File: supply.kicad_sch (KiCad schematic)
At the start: 64 parts, among them J3 Molex_Nano-Fit_1x2_SMD_105430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, Q2 SSM3J332R, Q3 SSM3J332R, Q4 BCM857BS-7-F, Q5 BCM857BS-7-F, Q6 SSM3J332R, Q8 PJE138K, Q9 SSM3J332R, U1 TPS56C230

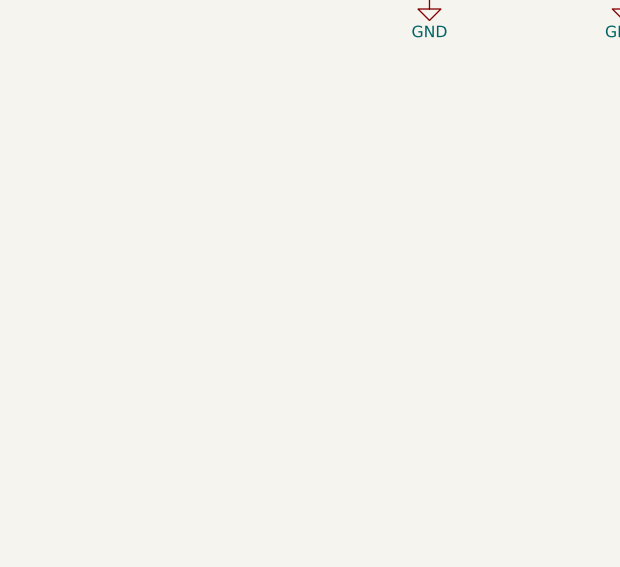
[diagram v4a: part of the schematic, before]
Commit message: [#54474] Change sheet placement in top sheet
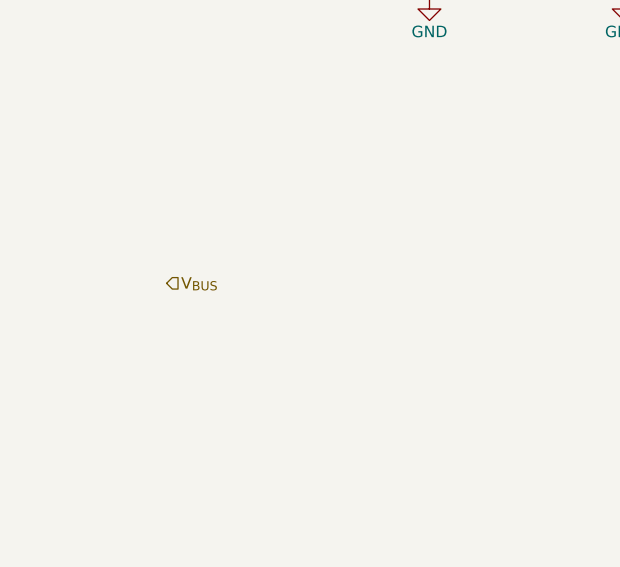
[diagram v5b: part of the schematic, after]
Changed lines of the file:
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@@
     (effects (font (size 1.27 1.27)) (justify right))
+  )
+  (hierarchical_label "V_{BUS}" (shape input) (at 29.21 231.14 0)
+    (effects (font (size 1.27 1.27)) (justify left))
   )
   (hierarchical_label "NVMe_EN" (shape input) (at 294.64 182.88 180)

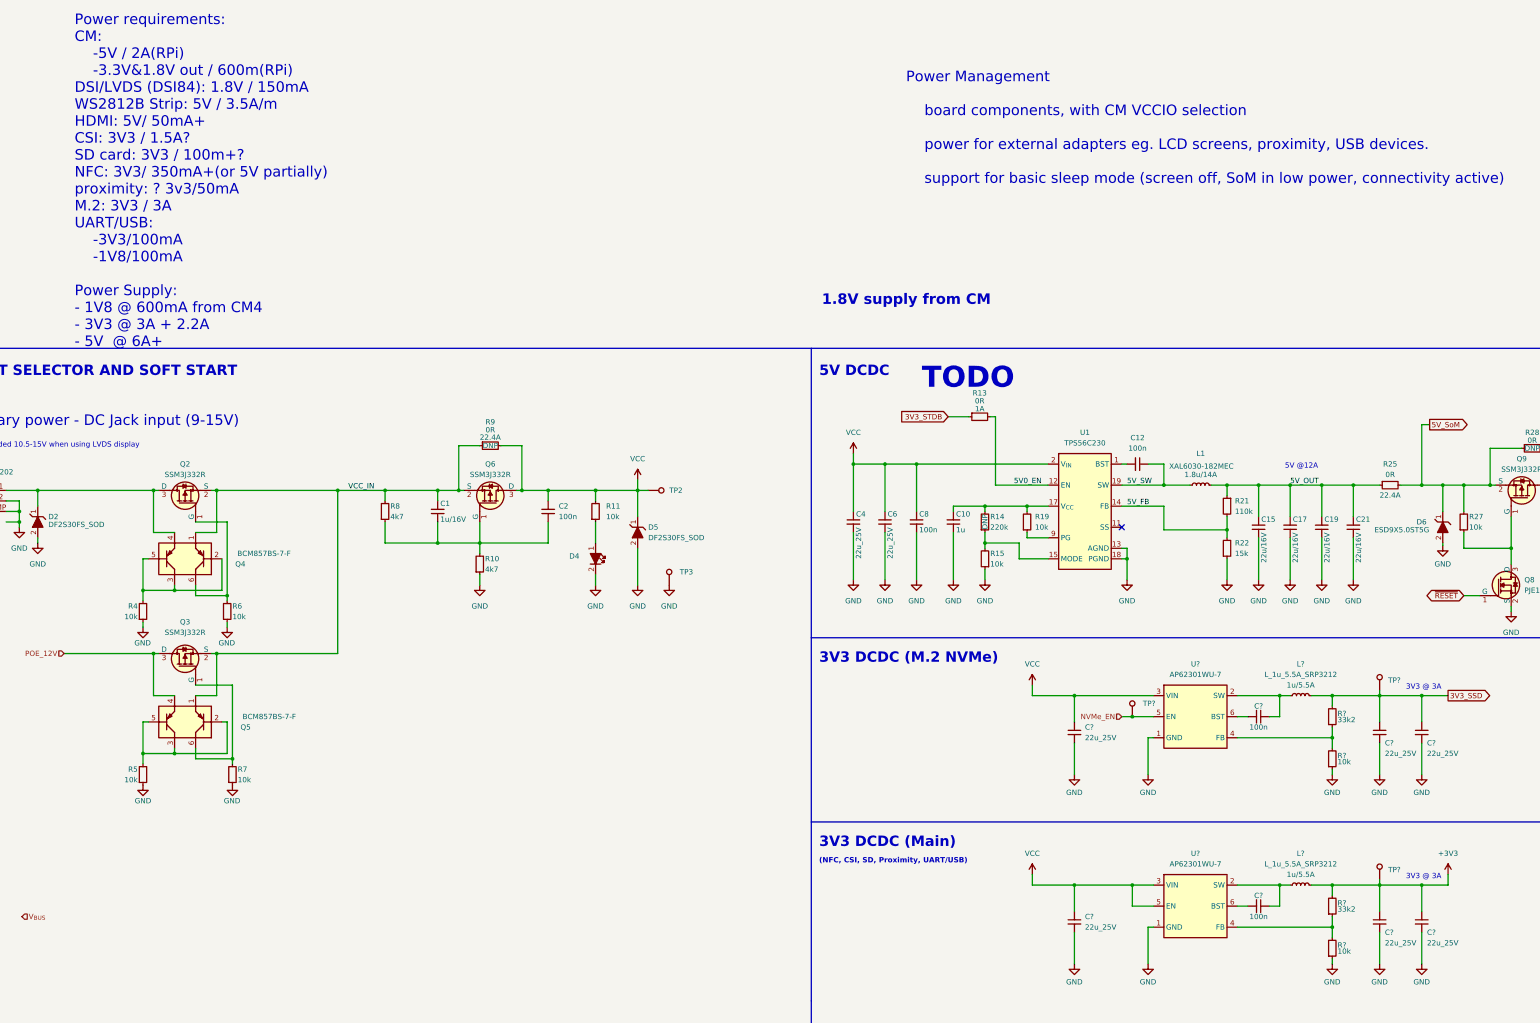
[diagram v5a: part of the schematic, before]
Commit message: [#54476] Update note about power requirements
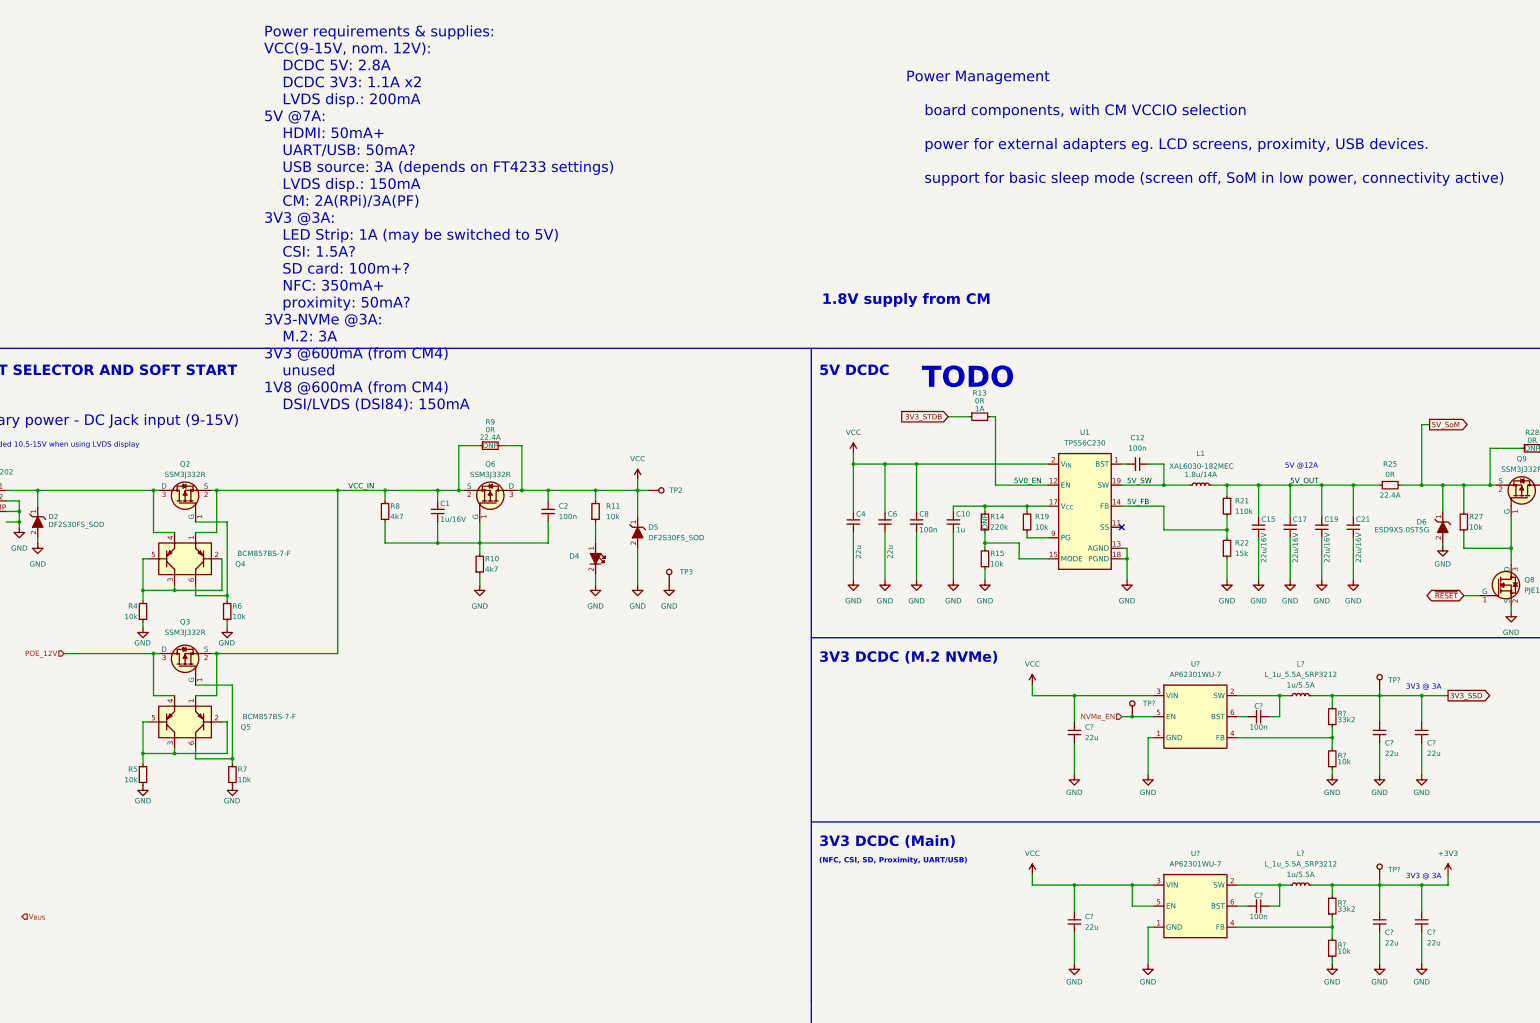
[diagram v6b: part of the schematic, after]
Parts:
- C4, C6, C? (x6): Dielectric (none) -> X5R; Manufacturer Samsung -> Samsung Electro-Mechanics; Val 22u_25V -> 22u; Voltage (none) -> 25V
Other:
- note added: "Power requirements & supplies: VCC(9-15V, nom. 12V): DCDC 5V: 2.8A DCDC 3V3: 1.1A x2 LVDS disp.: 200mA 5V @7A: HDMI: 50mA+ UART/USB: 50mA? USB source: 3A (depends on FT4233 settings) LVDS disp.: 150mA CM: 2A(RPi)/3A(PF) 3V3 @3A: LED Strip: 1A (may be switched to 5V) CSI: 1.5A? SD card: 100m+? NFC: 350mA+ proximity: 50mA? 3V3-NVMe @3A: M.2: 3A 3V3 @600mA (from CM4) unused 1V8 @600mA (from CM4) DSI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"
- note removed: "Power requirements: CM: -5V / 2A(RPi) -3.3V&1.8V out / 600m(RPi) DSI/LVDS (DSI84): 1.8V / 150mA WS2812B Strip: 5V / 3.5A/m HDMI: 5V/ 50mA+ CSI: 3V3 / 1.5A? SD card: 3V3 / 100m+? NFC: 3V3/ 350mA+(or 5V partially) proximity: ? 3v3/50mA M.2: 3V3 / 3A UART/USB: -3V3/100mA -1V8/100mA Power Supply: - 1V8 @ 600mA from CM4 - 3V3 @ 3A + 2.2A - 5V @ 6A+"

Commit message: [#54476] Complete power supply
- add USB-PD input
- change DCDC 5V
- add power indicators
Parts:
- removed C10: C_1u_0402, antmicro-footprints:C_0402_1005Metric, symbol antmicroCapacitors0402:C_1u_0402
- removed C12, C8: C_100n_0402, antmicro-footprints:C_0402_1005Metric, symbol antmicroCapacitors0402:C_100n_0402
- removed C15, C17, C19, C21: C_22u_16V_0603, antmicro-footprints:C_0603_1608Metric, symbol antmicroCapacitors0603:C_22u_16V_0603
- removed C4, C6, C? (x6): C_22u_25V_0805, antmicro-footprints:C_0805_2012Metric, symbol antmicroCapacitorsmisc:C_22u_25V_0805
- removed D6: ESD9X5.0ST5G, antmicro-footprints:SOD-923, symbol antmicroTVSDiodes:ESD9X5.0ST5G
- removed L1: L_1u8_14A_Coilcraft-XAL6030, antmicro-footprints:L_Coilcraft-XAL6030, symbol antmicroFixedInductors:L_1u8_14A_Coilcraft-XAL6030
- removed Q2, Q3, Q6, Q9: SSM3J332R, antmicro-footprints:SOT-23-3, symbol antmicroTransistorsFETsMOSFETsSingle:SSM3J332R
- removed Q8: PJE138K, antmicro-footprints:SOT-523, symbol antmicroTransistorsFETsMOSFETsSingle:PJE138K
- removed R13: R_0R_0402, antmicro-footprints:R_0402_1005Metric, symbol antmicroResistors0402:R_0R_0402
- removed R14: R_220k_0402, antmicro-footprints:R_0402_1005Metric, symbol antmicroResistors0402:R_220k_0402
- removed R15, R19, R27: R_10k_0402, antmicro-footprints:R_0402_1005Metric, symbol antmicroResistors0402:R_10k_0402
- removed R21: R_110k_0402, antmicro-footprints:R_0402_1005Metric, symbol antmicroResistors0402:R_110k_0402
- removed R22: R_15k_0402, antmicro-footprints:R_0402_1005Metric, symbol antmicroResistors0402:R_15k_0402
- removed R25, R28: R_0R_22.4A_0603, antmicro-footprints:R_0603_1608Metric, symbol antmicroResistors0603:R_0R_22.4A_0603
- removed TP5: TP_0.75mm_SMD, antmicro-footprints:TP_SMD_0.75mm, symbol antmicroTestPoints:TP_0.75mm_SMD
- removed TP? (x2): TP_1mm_SMD, antmicro-footprints:TP_SMD_1mm, symbol antmicroTestPoints:TP_1mm_SMD
- removed U1: TPS56C230, antmicro-footprints:QFN-20-1EP_3x3mm_P0.45mm, symbol antmicroDCDCConverters:TPS56C230
- added C? (x11): C_22u_25V_0805, antmicro-footprints:C_0805_2012Metric, symbol antmicroCapacitorsmisc:C_22u_25V_0805
- added C? (x2): C_100n_0402, antmicro-footprints:C_0402_1005Metric, symbol antmicroCapacitors0402:C_100n_0402
- added C?: C_1u_0402, antmicro-footprints:C_0402_1005Metric, symbol antmicroCapacitors0402:C_1u_0402
- added D? (x3): LED_G, antmicro-footprints:LED_0603_1608Metric_R, symbol antmicroLEDIndicationDiscrete:LED_R_0603_598-8D80-107F
- added L?: L_1u8_14A_Coilcraft-XAL6030, antmicro-footprints:L_Coilcraft-XAL6030, symbol antmicroFixedInductors:L_1u8_14A_Coilcraft-XAL6030
- added Q? (x4): SQS401EN-T1_BE3, antmicro-footprints:Vishay_PowerPAK_1212-8_Single, symbol antmicroTransistorsFETsMOSFETsSingle:SQS401EN-T1_BE3
- added Q?: BCM857BS-7-F, antmicro-footprints:SOT-363, symbol antmicroTransistorsBipolarArrays:BCM857BS-7-F
- added R?: R_1k_0402, antmicro-footprints:R_0402_1005Metric, symbol antmicroResistors0402:R_1k_0402
- added R? (x2): R_200R_0402, antmicro-footprints:R_0402_1005Metric, symbol antmicroResistors0402:R_200R_0402
- added R? (x3): R_0R_22.4A_0603, antmicro-footprints:R_0603_1608Metric, symbol antmicroResistors0603:R_0R_22.4A_0603
- added R? (x2): R_10k_0402, antmicro-footprints:R_0402_1005Metric, symbol antmicroResistors0402:R_10k_0402
- added R?: R_110k_0402, antmicro-footprints:R_0402_1005Metric, symbol antmicroResistors0402:R_110k_0402
- added R? (x2): R_100k_0402, antmicro-footprints:R_0402_1005Metric, symbol antmicroResistors0402:R_100k_0402
- added R?: R_15k_0402, antmicro-footprints:R_0402_1005Metric, symbol antmicroResistors0402:R_15k_0402
- added TP? (x6): TP_0.75mm_SMD, antmicro-footprints:TP_SMD_0.75mm, symbol antmicroTestPoints:TP_0.75mm_SMD
- added TP?: TP_1mm_SMD, antmicro-footprints:TP_SMD_1mm, symbol antmicroTestPoints:TP_1mm_SMD
- added U?: AP62600SJ-7, antmicro-footprints:V-QFN2030-12, symbol antmicroDCDCConverters:AP62600SJ-7
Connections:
- net +3V3: now also R?.2, R?.2, TP?.1; no longer L?.2, R?.2
- net +5V: now also R?.2, R?.2, TP?.1
- net 3V3_SSD: now also R?.2, R?.2, TP?.1; no longer L?.2, R?.2
- net GND: now also C?.1, C?.2, C?.2, C?.2, C?.2, C?.2, C?.2, C?.2, C?.2, C?.2, C?.2, C?.2, C?.2, D?.2, D?.2, D?.2, R?.1, R?.1, R?.1, TP?.1, TP?.1, TP?.1, U?.1 (PGND), U?.11 (GND)
- net POE_12V: now also Q?.5 (D)
- net VCC: now also C?.1, C?.1, C?.1, C?.1, C?.1, Q?.5 (D), R?.2, U?.2 (VIN)
- net VCC_IN: now also Q?.1, Q?.1 (S), Q?.1 (S), Q?.1 (S), Q?.1 (S), Q?.2 (S), Q?.2 (S), Q?.2 (S), Q?.2 (S), Q?.3 (S), Q?.3 (S), Q?.3 (S), Q?.3 (S)
- net V_{BUS}: now also Q?.4, Q?.5 (D)
- net at Q4.6, R6.2: now also Q?.4 (G)
- net at C1.1, C2.1, R10.2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: now also Q?.4 (G)
- net at D2.1, J3.1, Q4.4: now also Q?.5 (D)
- net at Q5.6, R7.2: now also Q?.4 (G)
- new net: C?.1, C?.1, C?.1, L?.2, R?.1
- new net: C?.1, L?.1, R?.1, U?.8 (SW)
- new net: C?.2, U?.7 (BST)
- new net: C?.1, C?.1, L?.2, R?.1, R?.2 (x2)
- new net: C?.2, R?.1, U?.9 (VCC)
- new net: D?.1, R?.1 (x3)
- new net: Q?.4 (G), Q?.6, R?.2
- new net: Q?.2, Q?.3, Q?.5, R?.2
- new net: R?.2, R?.2, U?.12 (FB)
- new net: R?.1, U?.3 (EN)
- new net: R?.2, TP?.1, U?.6 (PG)
- no-connect marks 1 -> 3
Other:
- note added: "3V3 @3A: LED Strip: 1A (may be switched to 5V) CSI: 1.5A? SD card: 100m+? NFC: 350mA+ proximity: 50mA? 3V3-NVMe @3A: M.2: 3A 3V3 @600mA (from CM4) unused 1V8 @600mA (from CM4) DSI/LVDS (DSI84): 150mA"
- note added: "5V @ 6A"
- note added: "Input selector & soft start"
- note added: "Power requirements & supplies:"
- note added: "VCC(9-15V, nom. 12V): DCDC 5V: 2.8A DCDC 3V3: 1.1A x2 LVDS disp.: 200mA 5V @6A: HDMI: 50mA+ UART/USB: 50mA? USB source: 3A (depends on FT4233 settings) LVDS disp.: 150mA CM: 2A(RPi)/3A(PF)"
- note removed: "1.8V supply from CM"
- note removed: "5V @12A"
- note removed: "INPUT SELECTOR AND SOFT START"
- note removed: "Power Management board components, with CM VCCIO selection power for external adapters eg. LCD screens, proximity, USB devices. support for basic sleep mode (screen off, SoM in low power, connectivity active)"
- note removed: "Power requirements & supplies: VCC(9-15V, nom. 12V): DCDC 5V: 2.8A DCDC 3V3: 1.1A x2 LVDS disp.: 200mA 5V @7A: HDMI: 50mA+ UART/USB: 50mA? USB source: 3A (depends on FT4233 settings) LVDS disp.: 150mA CM: 2A(RPi)/3A(PF) 3V3 @3A: LED Strip: 1A (may be switched to 5V) CSI: 1.5A? SD card: 100m+? NFC: 350mA+ proximity: 50mA? 3V3-NVMe @3A: M.2: 3A 3V3 @600mA (from CM4) unused 1V8 @600mA (from CM4) DSI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"
- note removed: "TODO"
- moved on the sheet: C1, C2, C?, D2, D4, D5, J3, L?, Q4, Q5, R10, R11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

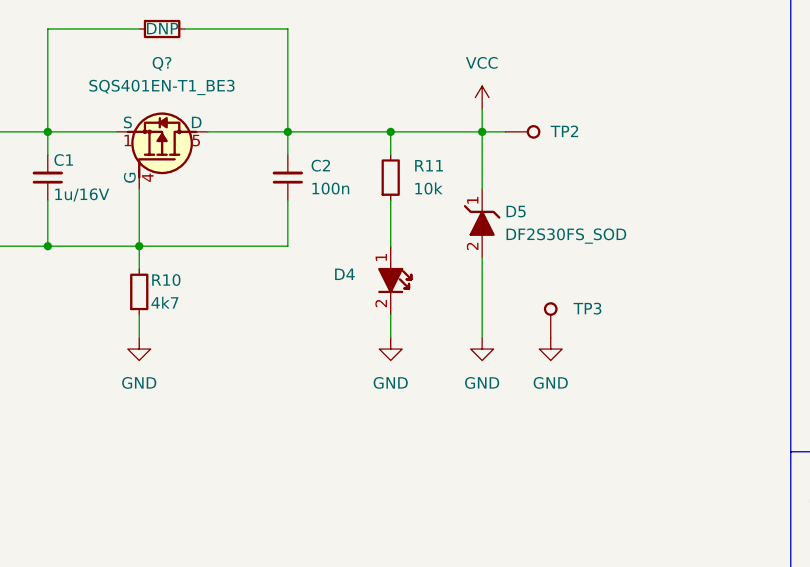
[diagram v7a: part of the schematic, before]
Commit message: [#54617] Uniform diodes MPN
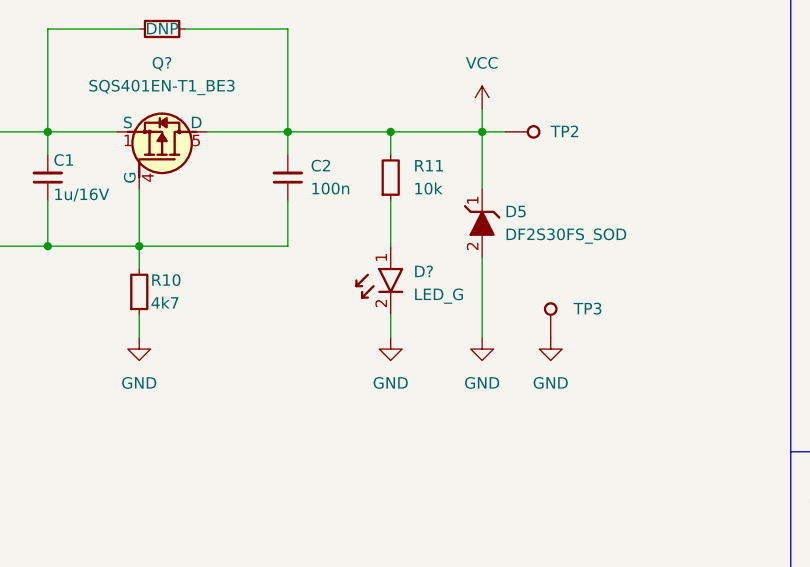
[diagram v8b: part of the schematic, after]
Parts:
- removed D4: LED_G_0603_LTST-C190GKT, antmicro-footprints:LED_0603_1608Metric_G, symbol antmicroLEDIndicationDiscrete:LED_G_0603_LTST-C190GKT
- added D?: LED_G, antmicro-footprints:LED_0603_1608Metric_R, symbol antmicroLEDIndicationDiscrete:LED_R_0603_598-8D80-107F
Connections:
- net GND: now also D?.2
- net at R11.1: now also D?.1
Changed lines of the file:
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@@
     (pin "1")
+  )
+  (symbol (lib_id "antmicroLEDIndicationDiscrete:LED_R_0603_598-8D80-107F") (at 175.26 134.62 90) (mirror x) (unit 1)
+    (in_bom yes) (on_board yes) (fields_autoplaced)
+    (property "Reference" "D?" (id 0) (at 177.8 137.4774 90)
+      (effects (font (size 1.27 1.27) (thickness 0.15)) (justify right))
+    )
+    (property "Value" "LED_G" (id 1) (at 177.8 140.0174 90)
+      (effects (font (size 1.27 1.27) (thickness 0.15)) (justify right))
+    )
+    (property "Footprint" "antmicro-footprints:LED_0603_1608Metric_R" (id 2) (at 182.88 157.48 0)
+      (effects (font (size 1.27 1.27) (thickness 0.15)) (justify left bottom) hide)
+    )
+    (property "Datasheet" "https://www.farnell.com/datasheets/3093797.pdf" (id 3) (at 185.42 157.48 0)
+      (effects (font (size 1.27 1.27) (thickness 0.15)) (justify left bottom) hide)
+    )
+    (property "MPN" "598-8D80-107F" (id 4) (at 170.18 140.0174 90)
+      (effects (font (size 1.27 1.27) (thickness 0.15)) (justify left) hide)
+    )
+    (property "Manufacturer" "Dialight" (id 5) (at 190.5 157.48 0)
+      (effects (font (size 1.27 1.27) (thickness 0.15)) (justify left bottom) hide)
+    )
+    (property "Author" "Antmicro" (id 6) (at 193.04 157.48 0)
+      (effects (font (size 1.27 1.27) (thickness 0.15)) (justify left bottom) hide)
+    )
+    (property "License" "Apache-2.0" (id 7) (at 195.58 157.48 0)
+      (effects (font (size 1.27 1.27) (thickness 0.15)) (justify left bottom) hide)
+    )
+    (pin "1")
+    (pin "2")
   )
   (symbol (lib_id "antmicropower:GND") (at 193.04 144.78 0) (mirror y) (unit 1)
@@
     (pin "6")
   )
-  (symbol (lib_id "antmicroLEDIndicationDiscrete:LED_G_0603_LTST-C190GKT") (at 175.26 134.62 270) (unit 1)
-    (in_bom yes) (on_board yes)
-    (property "Reference" "D4" (id 0) (at 168.91 137.795 90)
-      (effects (font (size 1.27 1.27)) (justify left))
-    )
-    (property "Value" "LED_G_0603_LTST-C190GKT" (id 1) (at 171.45 134.62 0)
-      (effects (font (size 1.27 1.27)) (justify left bottom) hide)
-    )
-    (property "Footprint" "antmicro-footprints:LED_0603_1608Metric_G" (id 2) (at 180.34 139.7 0)
-      (effects (font (size 1.524 1.524)) (justify left bottom) hide)
-    )
-    (property "Datasheet" "https://media.digikey.com/pdf/Data%20Sheets/Lite-On%20PDFs/LTST-C190GKT.pdf" (id 3) (at 182.88 139.7 0)
-      (effects (font (size 1.524 1.524)) (justify left bottom) hide)
-    )
-    (property "MPN" "LTST-C190GKT" (id 4) (at 187.96 139.7 0)
-      (effects (font (size 1.524 1.524)) (justify left bottom) hide)
-    )
-    (property "Manufacturer" "Lite-On Inc." (id 5) (at 203.2 139.7 0)
-      (effects (font (size 1.524 1.524)) (justify left bottom) hide)
-    )
-    (property "Author" "Antmicro" (id 6) (at 154.94 157.48 0)
-      (effects (font (size 1.27 1.27) (thickness 0.15)) (justify left bottom) hide)
-    )
-    (property "License" "Apache-2.0" (id 7) (at 152.4 157.48 0)
-      (effects (font (size 1.27 1.27) (thickness 0.15)) (justify left bottom) hide)
-    )
-    (pin "1")
-    (pin "2")
-  )
   (symbol (lib_id "antmicropower:GND") (at 87.63 242.57 0) (unit 1)
